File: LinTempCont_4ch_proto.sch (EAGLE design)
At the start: 194 parts, among them IC1 LM393D, IC10 AD5262, IC2 LM393D, IC3 AD5624R, IC4 AD5262, IC5 AD5262, IC7 LM393D, IC8 AD5262, IC9 LM393D, T1 MMBT3904, T2 MMBT3904, T3 MMBT3904, T4 MMBT3904, T5 MMBT3904, T6 MMBT3904, T7 MMBT3904, T8 MMBT3904, X1 BNC-H, X2 BNC-H, X3 BNC-H, X4 BNC-H, X5 BNC-H, X6 BNC-H, X7 BNC-H, X8 BNC-H

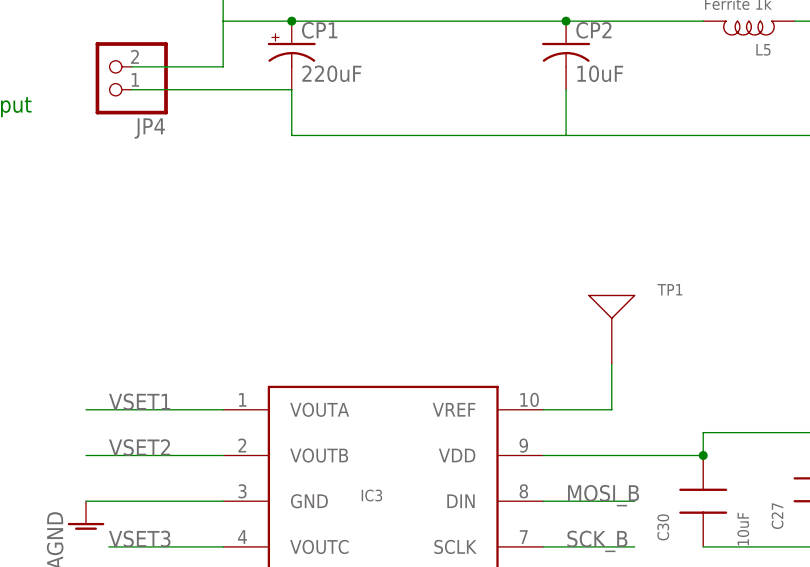
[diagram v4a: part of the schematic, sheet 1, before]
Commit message: Add DAC Vref Jumper/Silkscreen Cleanup
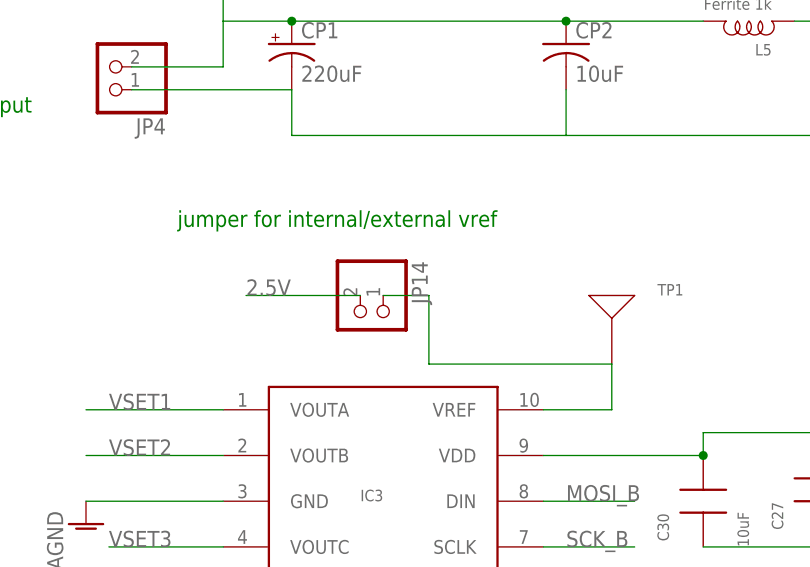
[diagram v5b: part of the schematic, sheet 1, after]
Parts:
- added JP14: (no value), pinhead:PINHD-1X2
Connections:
- net 2.5V: now also JP14.2
- net N$1: now also JP14.1
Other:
- note added: "jumper for internal/external vref"
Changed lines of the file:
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@@
 <part name="TP27" library="Lin-Temp-Controller" deviceset="TESTPT" device=""/>
 <part name="AGND43" library="supply1" deviceset="AGND" device=""/>
+<part name="JP14" library="pinhead" deviceset="PINHD-1X2" device=""/>
 </parts>
 <sheets>
@@
 <text x="332.74" y="95.25" size="1.778" layer="91">+5V filtered</text>
 <text x="215.9" y="88.9" size="1.778" layer="91">5V input</text>
+<text x="241.3" y="76.2" size="1.778" layer="91">jumper for internal/external vref</text>
 </plain>
 <instances>
@@
 <instance part="TP27" gate="G$1" x="193.04" y="-27.94"/>
 <instance part="AGND43" gate="VR1" x="193.04" y="-35.56"/>
+<instance part="JP14" gate="G$1" x="261.62" y="66.04" rot="R270"/>
 </instances>
 <busses>
@@
 <pinref part="TP7" gate="G$1" pin="P$1"/>
 </segment>
+<segment>
+<pinref part="JP14" gate="G$1" pin="2"/>
+<wire x1="261.62" y1="68.58" x2="248.92" y2="68.58" width="0.1524" layer="91"/>
+<label x="248.92" y="68.58" size="1.778" layer="95"/>
+</segment>
 </net>
 <net name="SCK_B" class="0">
@@
 <pinref part="TP1" gate="G$1" pin="P$1"/>
 <wire x1="289.56" y1="55.88" x2="289.56" y2="60.96" width="0.1524" layer="91"/>
-</segment>
-</net>
+<wire x1="289.56" y1="60.96" x2="269.24" y2="60.96" width="0.1524" layer="91"/>
+<wire x1="269.24" y1="60.96" x2="269.24" y2="68.58" width="0.1524" layer="91"/>
+<pinref part="JP14" gate="G$1" pin="1"/>
+<wire x1="269.24" y1="68.58" x2="264.16" y2="68.58" width="0.1524" layer="91"/>
+</segment>
+</net>

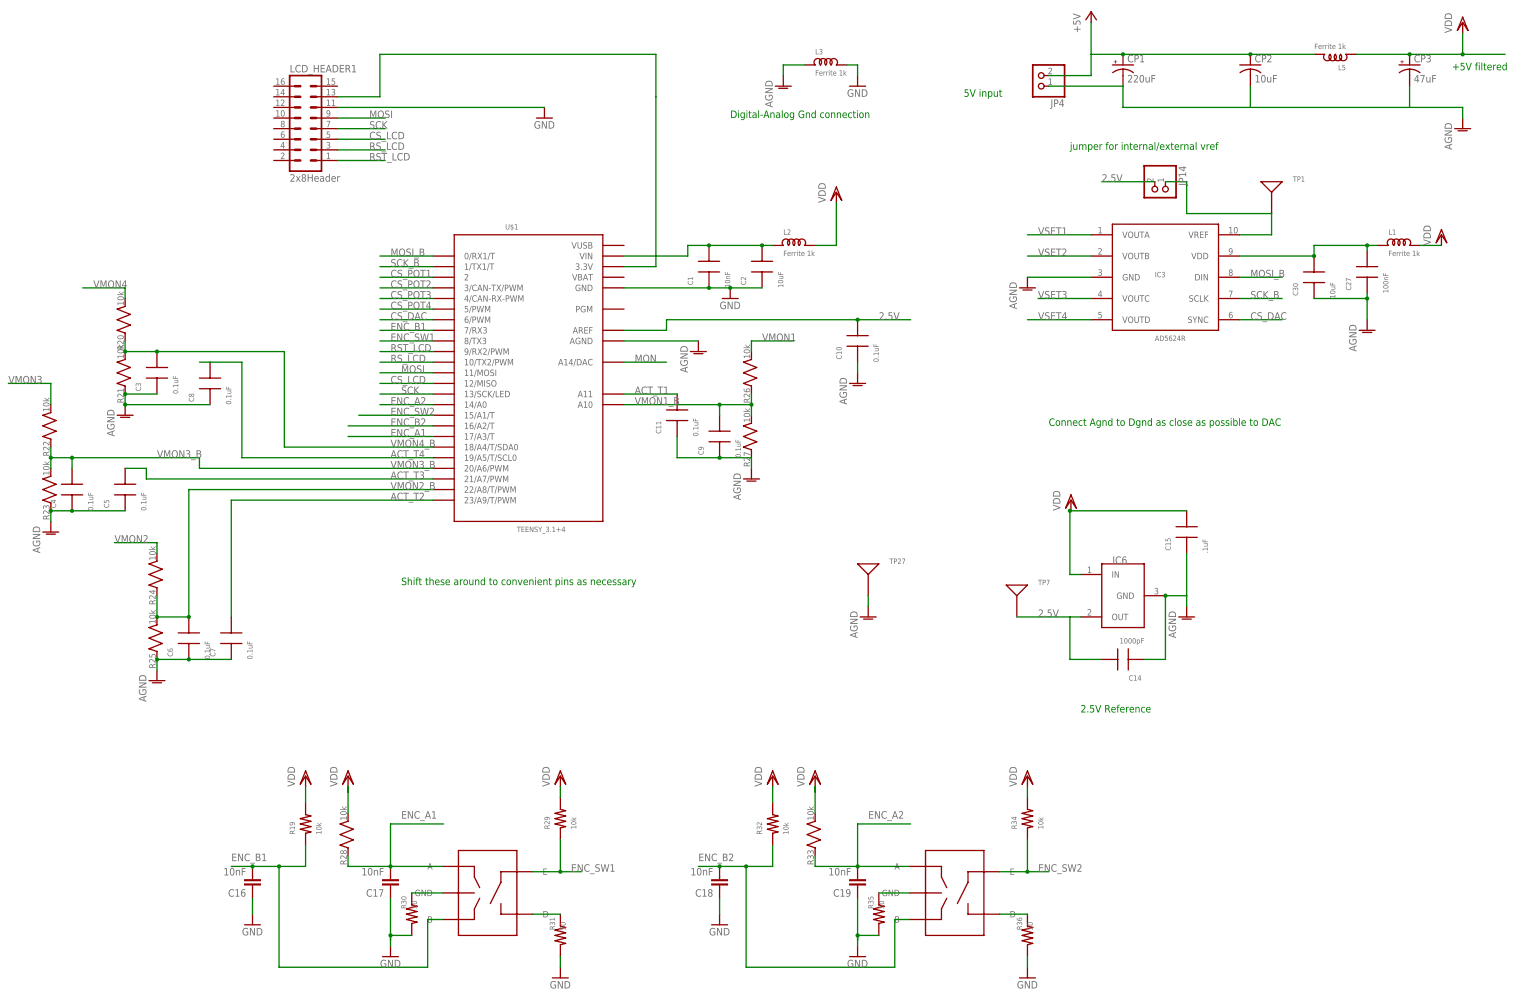
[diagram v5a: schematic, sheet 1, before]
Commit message: Add BOM, minor updates to reflect part availability
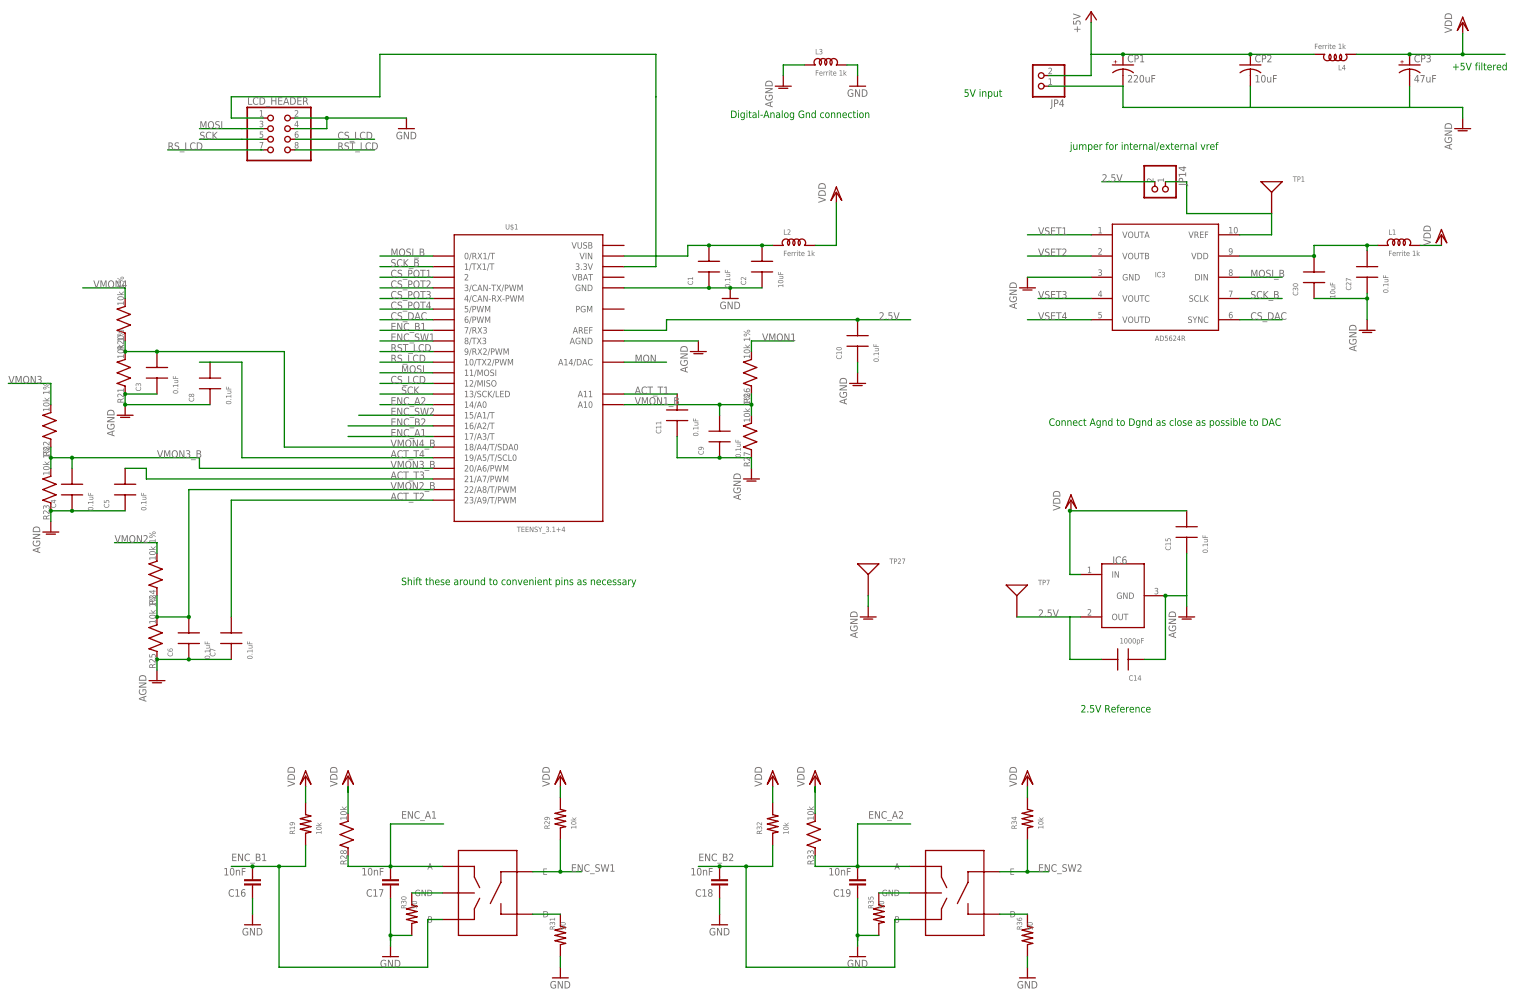
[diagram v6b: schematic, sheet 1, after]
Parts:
- removed LCD_HEADER1: 2x8Header, mcu-accessories:ML16
- added LCD_HEADER: (no value), mcu-accessories:PINHD-2X4-SHROUD
- C1: value 10nF -> 0.1uF
- C12, C20, C22, C24, C27: value 100nF -> 0.1uF
- C13, C2, C21, C23, C25, C30: device rlc-jqi:CAP0603 -> rlc-jqi:CAP0805
- C15: value .1uF -> 0.1uF
- R20, R21, R22, R23, R24, R25, R26, R27: value 10k -> 10k 1%
- renumbered L5 to L4
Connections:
- net 3.3V: now also LCD_HEADER.1; no longer LCD_HEADER1.13
- net CS_LCD: now also LCD_HEADER.6; no longer LCD_HEADER1.5
- net DGND: now also LCD_HEADER.2, LCD_HEADER.4; no longer LCD_HEADER1.11
- net MOSI: now also LCD_HEADER.3; no longer LCD_HEADER1.9
- net RST_LCD: now also LCD_HEADER.8; no longer LCD_HEADER1.1
- net RS_LCD: now also LCD_HEADER.7; no longer LCD_HEADER1.3
- net SCK: now also LCD_HEADER.5; no longer LCD_HEADER1.7

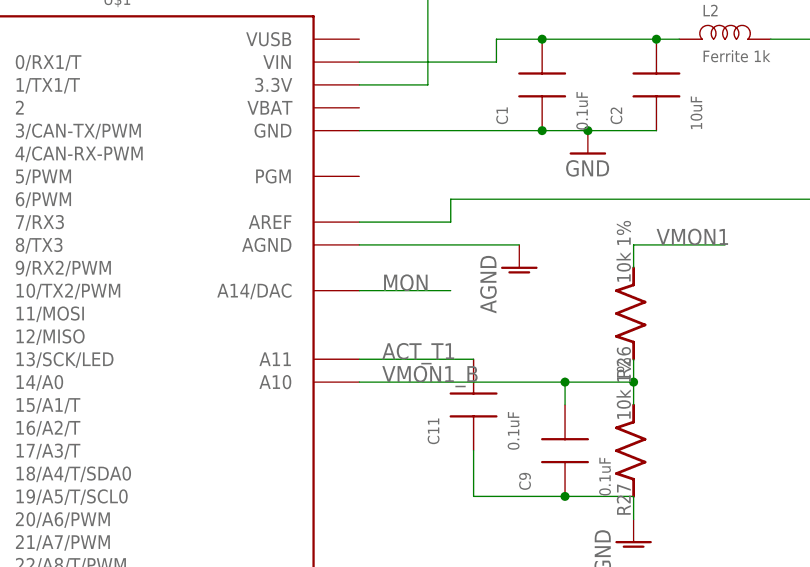
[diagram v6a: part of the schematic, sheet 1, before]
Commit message: Prepare for ordering boards
Update BOM, minor changes to board to move header slightly, ensure
silkscreen is using vector fonts
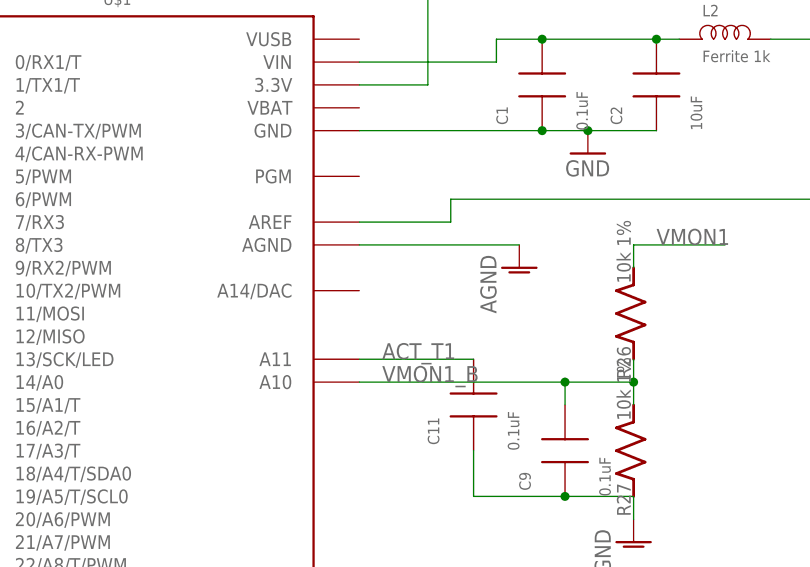
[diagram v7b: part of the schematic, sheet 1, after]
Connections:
- removed net MON: U$1.A14/DAC
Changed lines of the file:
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@@
 <grid distance="0.1" unitdist="inch" unit="inch" style="lines" multiple="1" display="no" altdistance="0.01" altunitdist="inch" altunit="inch"/>
 <layers>
-<layer number="1" name="Top" color="4" fill="1" visible="yes" active="no"/>
-<layer number="2" name="Route2" color="1" fill="3" visible="yes" active="no"/>
-<layer number="3" name="Route3" color="4" fill="3" visible="yes" active="no"/>
-<layer number="4" name="Route4" color="1" fill="4" visible="yes" active="no"/>
-<layer number="5" name="Route5" color="4" fill="4" visible="yes" active="no"/>
-<layer number="6" name="Route6" color="1" fill="8" visible="yes" active="no"/>
-<layer number="7" name="Route7" color="4" fill="8" visible="yes" active="no"/>
-<layer number="8" name="Route8" color="1" fill="2" visible="yes" active="no"/>
-<layer number="9" name="Route9" color="4" fill="2" visible="yes" active="no"/>
-<layer number="10" name="Route10" color="1" fill="7" visible="yes" active="no"/>
-<layer number="11" name="Route11" color="4" fill="7" visible="yes" active="no"/>
-<layer number="12" name="Route12" color="1" fill="5" visible="yes" active="no"/>
-<layer number="13" name="Route13" color="4" fill="5" visible="yes" active="no"/>
-<layer number="14" name="Route14" color="1" fill="6" visible="yes" active="no"/>
-<layer number="15" name="Route15" color="4" fill="6" visible="yes" active="no"/>
-<layer number="16" name="Bottom" color="1" fill="1" visible="yes" active="no"/>
-<layer number="17" name="Pads" color="2" fill="1" visible="yes" active="no"/>
-<layer number="18" name="Vias" color="2" fill="1" visible="yes" active="no"/>
-<layer number="19" name="Unrouted" color="6" fill="1" visible="yes" active="no"/>
-<layer number="20" name="Dimension" color="15" fill="1" visible="yes" active="no"/>
-<layer number="21" name="tPlace" color="7" fill="1" visible="yes" active="no"/>
-<layer number="22" name="bPlace" color="7" fill="1" visible="yes" active="no"/>
-<layer number="23" name="tOrigins" color="15" fill="1" visible="yes" active="no"/>
-<layer number="24" name="bOrigins" color="15" fill="1" visible="yes" active="no"/>
-<layer number="25" name="tNames" color="7" fill="1" visible="yes" active="no"/>
-<layer number="26" name="bNames" color="7" fill="1" visible="yes" active="no"/>
-<layer number="27" name="tValues" color="7" fill="1" visible="yes" active="no"/>
-<layer number="28" name="bValues" color="7" fill="1" visible="yes" active="no"/>
+<layer number="1" name="Top" color="4" fill="1" visible="no" active="no"/>
+<layer number="2" name="Route2" color="1" fill="3" visible="no" active="no"/>
+<layer number="3" name="Route3" color="4" fill="3" visible="no" active="no"/>
+<layer number="4" name="Route4" color="1" fill="4" visible="no" active="no"/>
+<layer number="5" name="Route5" color="4" fill="4" visible="no" active="no"/>
+<layer number="6" name="Route6" color="1" fill="8" visible="no" active="no"/>
+<layer number="7" name="Route7" color="4" fill="8" visible="no" active="no"/>
+<layer number="8" name="Route8" color="1" fill="2" visible="no" active="no"/>
+<layer number="9" name="Route9" color="4" fill="2" visible="no" active="no"/>
+<layer number="10" name="Route10" color="1" fill="7" visible="no" active="no"/>
+<layer number="11" name="Route11" color="4" fill="7" visible="no" active="no"/>
+<layer number="12" name="Route12" color="1" fill="5" visible="no" active="no"/>
+<layer number="13" name="Route13" color="4" fill="5" visible="no" active="no"/>
+<layer number="14" name="Route14" color="1" fill="6" visible="no" active="no"/>
+<layer number="15" name="Route15" color="4" fill="6" visible="no" active="no"/>
+<layer number="16" name="Bottom" color="1" fill="1" visible="no" active="no"/>
+<layer number="17" name="Pads" color="2" fill="1" visible="no" active="no"/>
+<layer number="18" name="Vias" color="2" fill="1" visible="no" active="no"/>
+<layer number="19" name="Unrouted" color="6" fill="1" visible="no" active="no"/>
+<layer number="20" name="Dimension" color="15" fill="1" visible="no" active="no"/>
+<layer number="21" name="tPlace" color="7" fill="1" visible="no" active="no"/>
+<layer number="22" name="bPlace" color="7" fill="1" visible="no" active="no"/>
+<layer number="23" name="tOrigins" color="15" fill="1" visible="no" active="no"/>
+<layer number="24" name="bOrigins" color="15" fill="1" visible="no" active="no"/>
+<layer number="25" name="tNames" color="7" fill="1" visible="no" active="no"/>
+<layer number="26" name="bNames" color="7" fill="1" visible="no" active="no"/>
+<layer number="27" name="tValues" color="7" fill="1" visible="no" active="no"/>
+<layer number="28" name="bValues" color="7" fill="1" visible="no" active="no"/>
 <layer number="29" name="tStop" color="7" fill="3" visible="no" active="no"/>
 <layer number="30" name="bStop" color="7" fill="6" visible="no" active="no"/>
@@
 <layer number="35" name="tGlue" color="7" fill="4" visible="no" active="no"/>
 <layer number="36" name="bGlue" color="7" fill="5" visible="no" active="no"/>
-<layer number="37" name="tTest" color="7" fill="1" visible="yes" active="no"/>
-<layer number="38" name="bTest" color="7" fill="1" visible="yes" active="no"/>
+<layer number="37" name="tTest" color="7" fill="1" visible="no" active="no"/>
+<layer number="38" name="bTest" color="7" fill="1" visible="no" active="no"/>
 <layer number="39" name="tKeepout" color="4" fill="11" visible="no" active="no"/>
 <layer number="40" name="bKeepout" color="1" fill="11" visible="no" active="no"/>
@@
 <layer number="44" name="Drills" color="7" fill="1" visible="no" active="no"/>
 <layer number="45" name="Holes" color="7" fill="1" visible="no" active="no"/>
-<layer number="46" name="Milling" color="3" fill="1" visible="yes" active="no"/>
-<layer number="47" name="Measures" color="7" fill="1" visible="yes" active="no"/>
-<layer number="48" name="Document" color="7" fill="1" visible="yes" active="no"/>
-<layer number="49" name="Reference" color="7" fill="1" visible="yes" active="no"/>
-<layer number="50" name="dxf" color="7" fill="1" visible="yes" active="no"/>
-<layer number="51" name="tDocu" color="7" fill="1" visible="yes" active="no"/>
-<layer number="52" name="bDocu" color="7" fill="1" visible="yes" active="no"/>
-<layer number="53" name="tGND_GNDA" color="7" fill="9" visible="yes" active="no"/>
-<layer number="54" name="bGND_GNDA" color="1" fill="9" visible="yes" active="no"/>
-<layer number="56" name="wert" color="7" fill="1" visible="yes" active="no"/>
-<layer number="57" name="tCAD" color="7" fill="1" visible="yes" active="no"/>
-<layer number="59" name="Invisible" color="7" fill="1" visible="yes" active="no"/>
-<layer number="60" name="bCarbon" color="7" fill="1" visible="yes" active="no"/>
-<layer number="61" name="stand" color="7" fill="1" visible="yes" active="no"/>
+<layer number="46" name="Milling" color="3" fill="1" visible="no" active="no"/>
+<layer number="47" name="Measures" color="7" fill="1" visible="no" active="no"/>
+<layer number="48" name="Document" color="7" fill="1" visible="no" active="no"/>
+<layer number="49" name="Reference" color="7" fill="1" visible="no" active="no"/>
+<layer number="50" name="dxf" color="7" fill="1" visible="no" active="no"/>
+<layer number="51" name="tDocu" color="7" fill="1" visible="no" active="no"/>
+<layer number="52" name="bDocu" color="7" fill="1" visible="no" active="no"/>
+<layer number="53" name="tGND_GNDA" color="7" fill="9" visible="no" active="no"/>
+<layer number="54" name="bGND_GNDA" color="1" fill="9" visible="no" active="no"/>
+<layer number="56" name="wert" color="7" fill="1" visible="no" active="no"/>
+<layer number="57" name="tCAD" color="7" fill="1" visible="no" active="no"/>
+<layer number="59" name="Invisible" color="7" fill="1" visible="no" active="no"/>
+<layer number="60" name="bCarbon" color="7" fill="1" visible="no" active="no"/>
+<layer number="61" name="stand" color="7" fill="1" visible="no" active="no"/>
 <layer number="90" name="Modules" color="5" fill="1" visible="no" active="no"/>
 <layer number="91" name="Nets" color="2" fill="1" visible="yes" active="yes"/>
@@
 </segment>
 </net>
-<net name="MON" class="0">
-<segment>
-<pinref part="U$1" gate="G$1" pin="A14/DAC"/>
-<wire x1="134.62" y1="25.4" x2="144.78" y2="25.4" width="0.1524" layer="91"/>
-<label x="137.16" y="25.4" size="1.778" layer="95"/>
-</segment>
-</net>
